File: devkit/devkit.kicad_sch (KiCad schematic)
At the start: 37 parts, among them J10 Conn_01x04, J12 Conn_01x22, J13 Conn_01x22, J14 Conn_01x20, J15 Conn_01x20, J16 Conn_01x03, J9 Conn_01x10, T10 TestPoint_Alt, U1 ESP32-S3-DevKitC, U2 RaspberryPi_Pico_W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

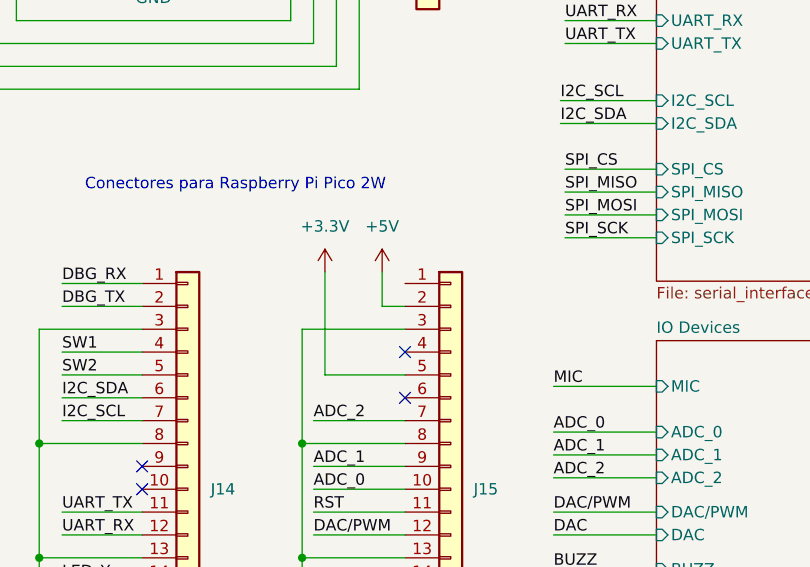
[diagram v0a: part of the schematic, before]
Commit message: chore: actualizo algunas huellas e info en pcb
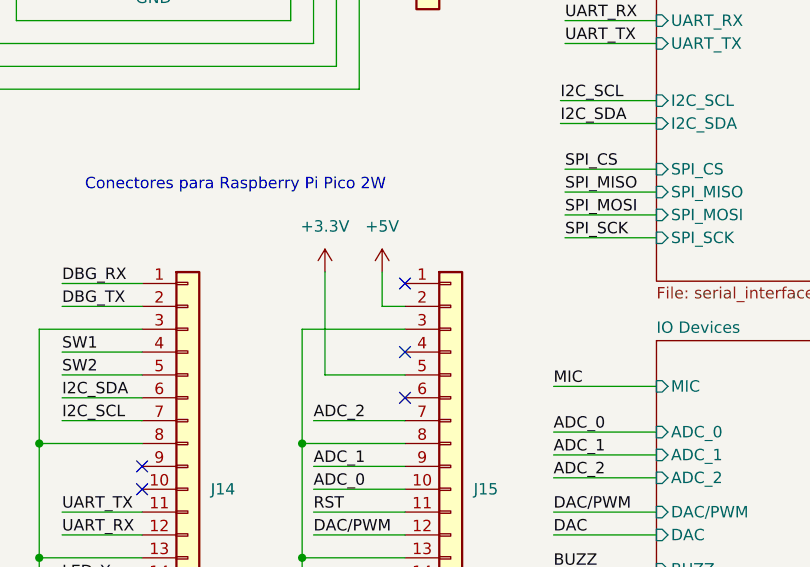
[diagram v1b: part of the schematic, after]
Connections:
- no-connect marks 47 -> 48
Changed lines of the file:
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@@
+	)
+	(no_connect
+		(at 220.98 105.41)
 	)
 	(no_connect
